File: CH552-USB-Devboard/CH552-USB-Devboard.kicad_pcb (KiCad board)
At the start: 2 copper layers, 22 x 40.5 mm, 28 parts, among them J1 Conn_01x11_Male, J2 Conn_01x11_Male, J3 USB_C_Receptacle, Q1 CPH6337, SW1 SW_Push, SW2 SW_Push, U1 CH552T, U2 CH552G, U3 MIC5504-3.3YM5, Y1 Crystal

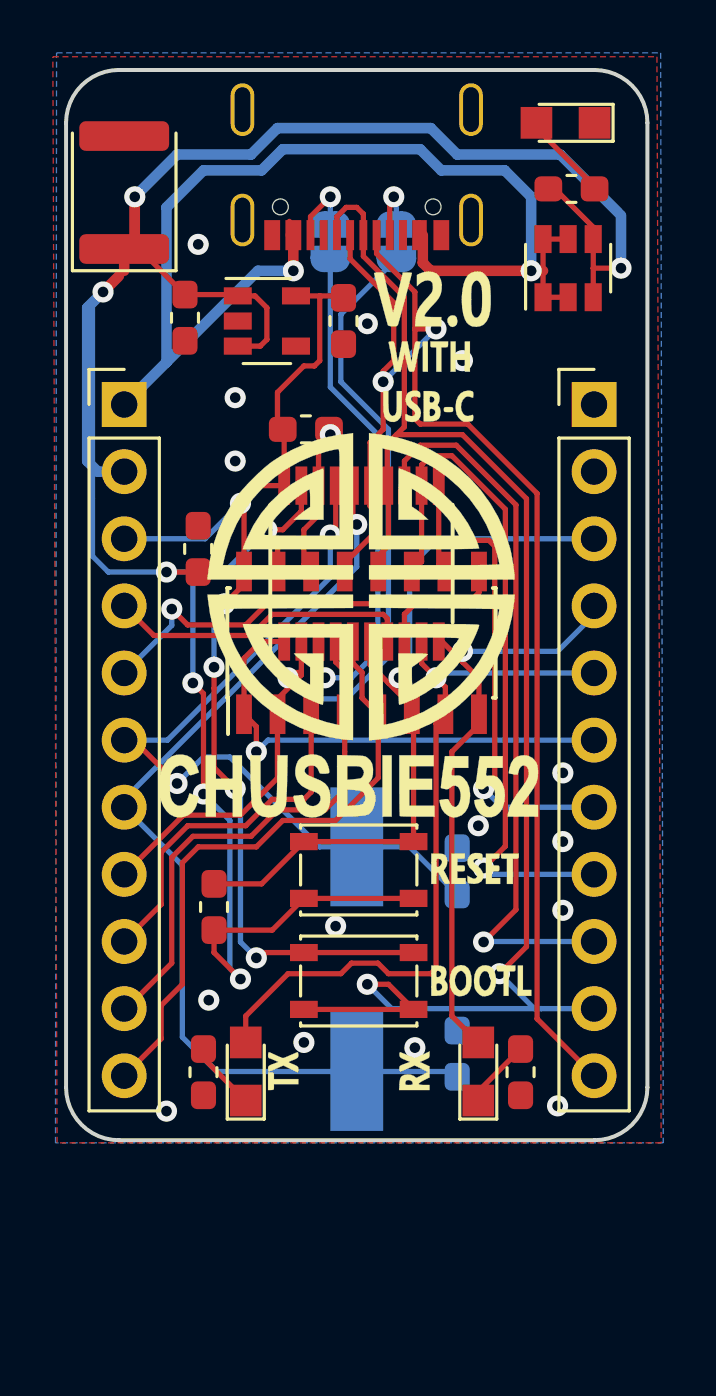
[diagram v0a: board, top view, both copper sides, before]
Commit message: add resistors for BOOTL and CC lines, remove LDO
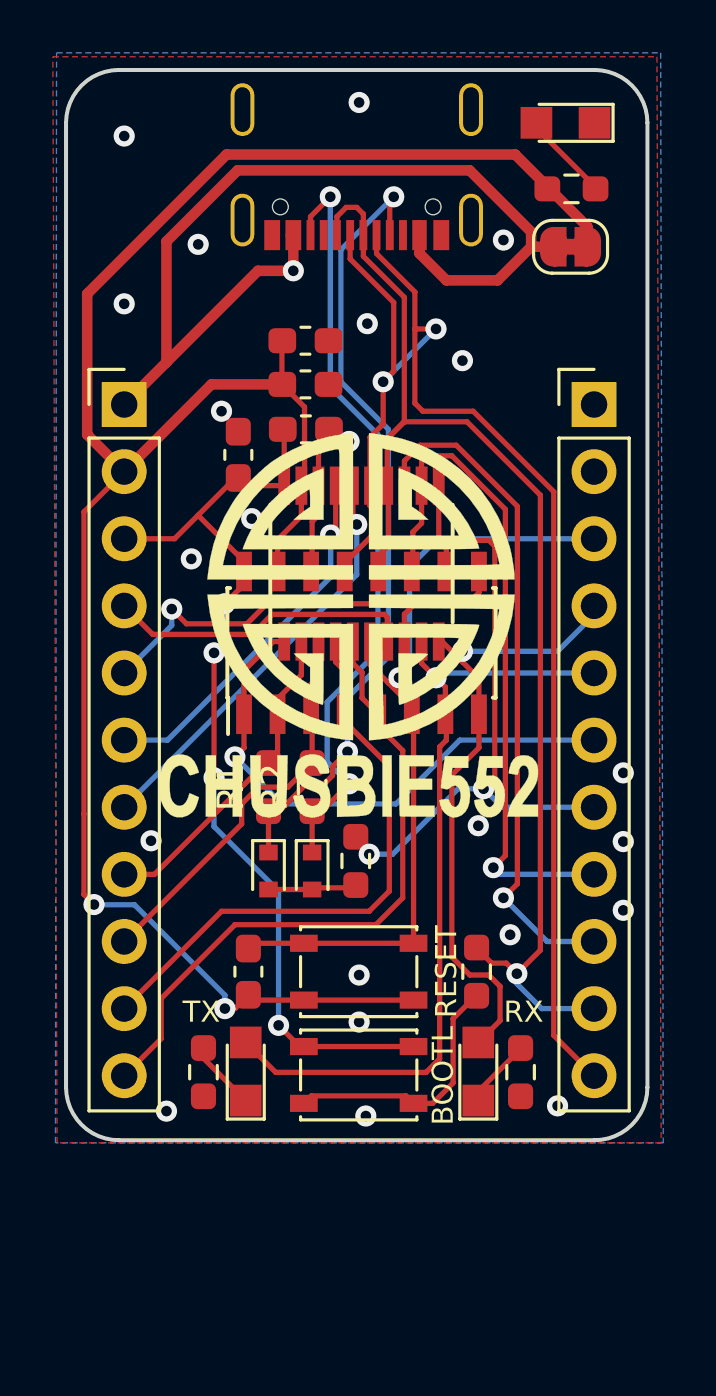
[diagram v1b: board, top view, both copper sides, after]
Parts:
- removed C5, C6: 100uF, Capacitor_SMD:C_0603_1608Metric_Pad1.05x0.95mm_HandSolder
- removed JP2: Jumper, Jumper:SolderJumper-2_P1.3mm_Bridged_RoundedPad1.0x1.5mm
- removed Q1: CPH6337, TO_SOT_Packages_SMD:SOT-23-6
- removed U3: MIC5504-3.3YM5, Package_TO_SOT_SMD:SOT-23-5
- removed Y1: Crystal, Crystal:Crystal_SMD_HC49-SD
- added D5: e.g. 1N4148, C917006, C708767, Diode_SMD:D_SOD-523, F.Cu at (83.3, 91.3)
- added R1: 68, Resistor_SMD:R_0603_1608Metric_Pad0.98x0.95mm_HandSolder, F.Cu at (81.7, 88.1)
- added R2: 68, Resistor_SMD:R_0603_1608Metric_Pad0.98x0.95mm_HandSolder, F.Cu at (83.3, 88.1)
- added R6: 22k, Resistor_SMD:R_0603_1608Metric_Pad0.98x0.95mm_HandSolder, F.Cu at (89.5, 95.1)
- added R7: 220, Resistor_SMD:R_0603_1608Metric_Pad0.98x0.95mm_HandSolder, F.Cu at (85.0, 90.9)
- C3: value 100uF -> 100nF
- C4, C7: value 1uF -> DNP/1uF
- D4: value D_ALT -> e.g. 1N4148, C917006, C708767; footprint Diode_SMD:D_1812_4532Metric -> Diode_SMD:D_SOD-523
- JP1: moved to F.Cu
- R3, R4: value 330r -> 1k; footprint Resistor_SMD:R_0603_1608Metric_Pad1.05x0.95mm_HandSolder -> Resistor_SMD:R_0603_1608Metric_Pad0.98x0.95mm_HandSolder
- R5: value 300r -> 1k; footprint Resistor_SMD:R_0603_1608Metric_Pad1.05x0.95mm_HandSolder -> Resistor_SMD:R_0603_1608Metric_Pad0.98x0.95mm_HandSolder
- moved D4 26.2 mm to (81.7, 91.3), turned to 270 degrees
- moved C1 7.43 mm to (83.1, 72.9), turned to 0 degrees
- moved JP1 6.59 mm to (93.1, 67.7), turned to 0 degrees
- moved C7 6.44 mm to (80.5, 75.6), turned to 90 degrees
- moved C4 4.64 mm to (83.1, 71.2), turned to 0 degrees
- moved SW2 3.85 mm to (85.1, 95.1)
- moved SW1 3.56 mm to (85.1, 99.0)
- moved C3 2.77 mm to (80.9, 95.1)
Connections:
- D4 pad 1: VCC -> /CC1
- D4 pad 2: GND -> Net-(D4-Pad2)
- J3 pad 1: GND -> (no net)
- JP1 pad 1: /CC1 -> VBUS
- JP1 pad 2: /P1.4 -> VCC
- SW1 pad 2: /P3.6 -> Net-(R6-Pad2)
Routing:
- net /CC1: track 2.75 -> 30.4 mm, vias 1 -> 2
- net /CC2: track 2.81 -> 29.3 mm, vias 1 -> 2
- net VCC: track 104.3 -> 78.9 mm, vias 8 -> 2
- net /P1.4: track 34.9 -> 12.3 mm, vias 1 -> 0
- net /P1.3: track 36.5 -> 15.9 mm
- net /P1.5: track 34.6 -> 15.1 mm, vias 1 -> 0
- net /P1.2: track 30.6 -> 13.9 mm, vias 2 -> 1
- net /P3.6: track 58.8 -> 47.9 mm, vias 2 -> 1
- net Net-(R6-Pad2): track 0.00 -> 9.89 mm
- net VBUS: track 46.0 -> 39.5 mm, vias 2 -> 1
- net /P3.3: track 19.4 -> 25.6 mm, vias 1 -> 2
- net +3V3: track 41.5 -> 36.0 mm, vias 5 -> 4
- net Net-(D4-Pad2): track 0.00 -> 3.38 mm
- net /P1.6: track 19.9 -> 22.2 mm
- net /P3.2: track 18.5 -> 20.7 mm
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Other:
- board text added: "BOOTL"
- board text added: "RESET"
- board text added: "RX"
- board text added: "TX"

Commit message: add reference voltage for ACMP, replace symbol for USB connector
That symbol was causing warnings because some of the pins are not
available on the footprint. Kicad has the appropriate symbol so
let's use that.
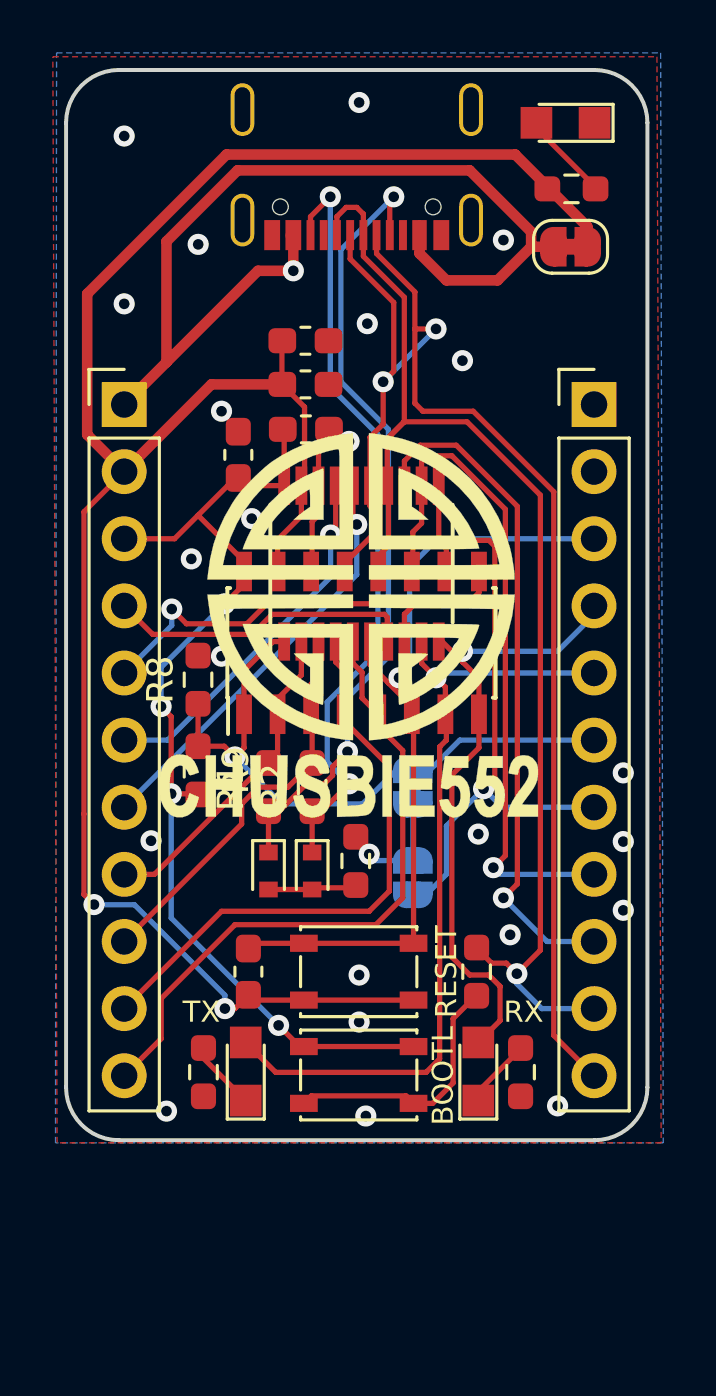
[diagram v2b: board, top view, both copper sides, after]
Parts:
- added JP2: Jumper, Jumper:SolderJumper-2_P1.3mm_Bridged_RoundedPad1.0x1.5mm, B.Cu at (87.1, 88.1)
- added JP3: Jumper, Jumper:SolderJumper-2_P1.3mm_Open_RoundedPad1.0x1.5mm, B.Cu at (87.1, 91.6)
- added R8: 1k, Resistor_SMD:R_0603_1608Metric_Pad0.98x0.95mm_HandSolder, F.Cu at (79.0, 84.1)
- added R9: 10k, Resistor_SMD:R_0603_1608Metric_Pad0.98x0.95mm_HandSolder, F.Cu at (79.0, 87.5)
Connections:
- R7 pad 1: /P3.3 -> Net-(JP2-Pad1)
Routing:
- net Net-(JP2-Pad1): track 0.00 -> 4.76 mm, vias 0 -> 1
- net /P3.2: track 20.7 -> 23.9 mm
- net +3V3: track 36.0 -> 38.7 mm
- net /P3.3: track 25.6 -> 24.8 mm, vias 2 -> 1
- net GND: vias 22 -> 23

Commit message: add voltage divider for VBUS, optimize GND plane
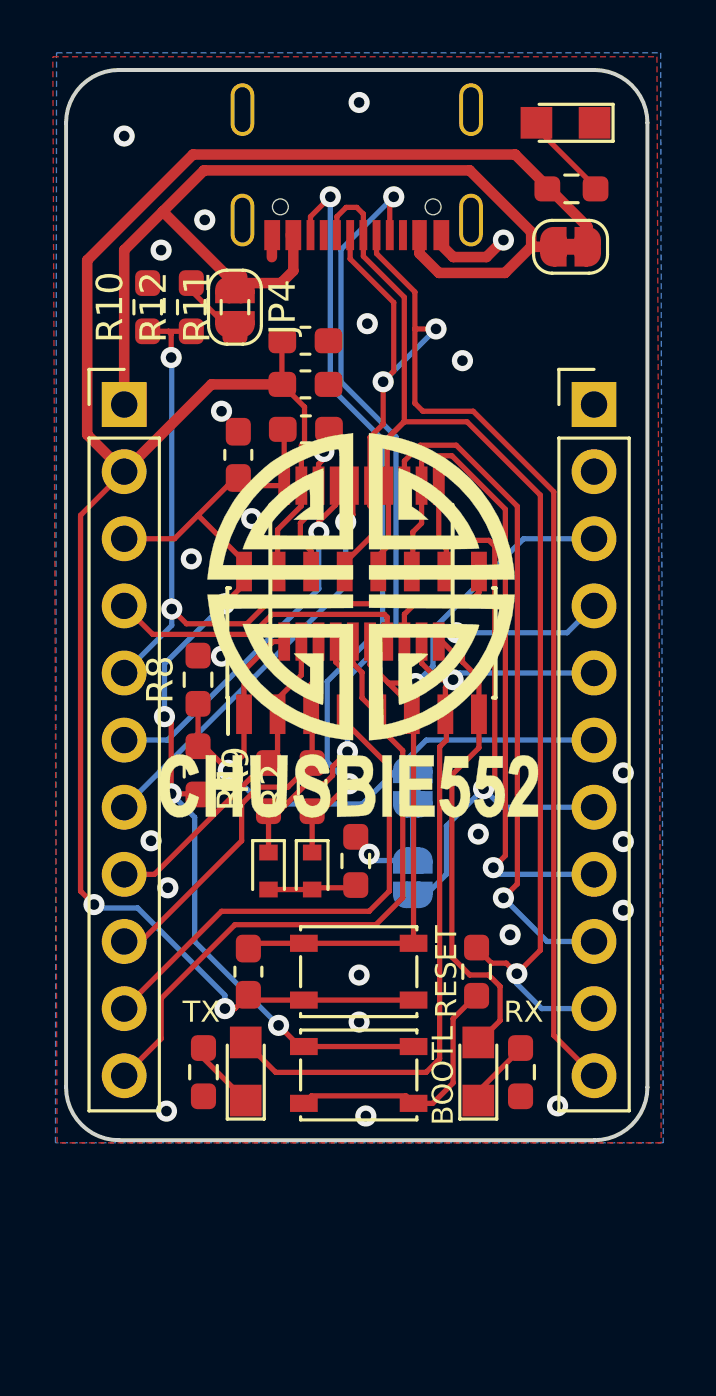
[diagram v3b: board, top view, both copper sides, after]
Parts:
- added JP4: Jumper, Jumper:SolderJumper-2_P1.3mm_Open_RoundedPad1.0x1.5mm, F.Cu at (80.4, 70.0)
- added R10: 1k, Resistor_SMD:R_0603_1608Metric_Pad0.98x0.95mm_HandSolder, F.Cu at (77.1, 70.0)
- added R11: 22k, Resistor_SMD:R_0603_1608Metric_Pad0.98x0.95mm_HandSolder, F.Cu at (80.4, 70.0)
- added R12: 22k, Resistor_SMD:R_0603_1608Metric_Pad0.98x0.95mm_HandSolder, F.Cu at (78.7, 70.0)
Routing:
- net /P1.1: track 17.9 -> 30.1 mm, vias 1 -> 2
- net GND: track 5.48 -> 9.82 mm, vias 23 -> 24
- net Net-(JP4-Pad2): track 0.00 -> 2.55 mm
- net /RESET: track 30.6 -> 29.2 mm
- net /P3.2: track 23.9 -> 25.0 mm
- net VCC: track 78.9 -> 79.7 mm
- net /P3.0: track 24.1 -> 24.6 mm
- net VBUS: track 39.5 -> 40.0 mm, vias 1 -> 0

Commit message: add 2nd USB connector, dedicated to PD monitoring
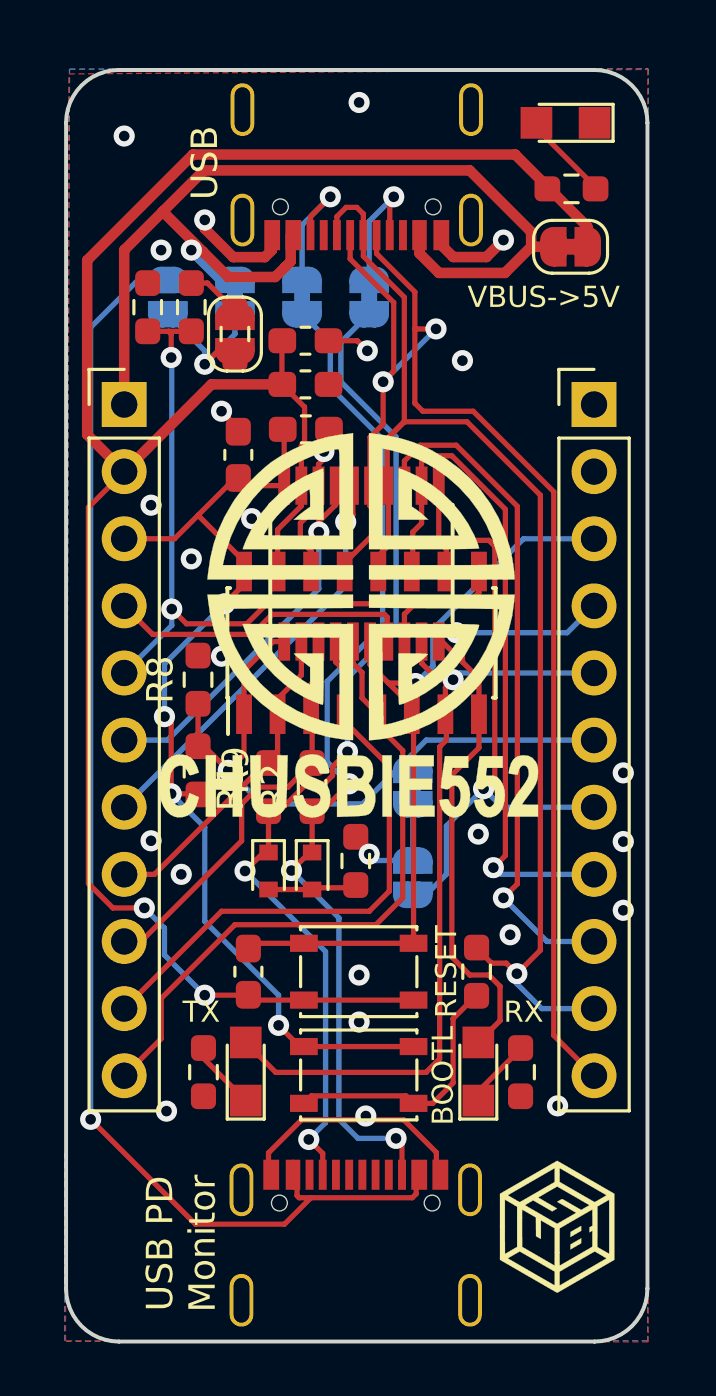
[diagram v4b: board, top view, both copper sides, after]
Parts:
- added G***: LOGO, Glowstone:subraum_8mm, B.Cu at (85.0, 105.0)
- added G***: LOGO, Glowstone:subraum_5mm, F.Cu at (92.6, 104.8)
- added J4: USB_C_Receptacle, footprint:VACON_CSP_USC16_TR, F.Cu at (85.0, 103.4)
- added JP5: Jumper, Jumper:SolderJumper-2_P1.3mm_Bridged_RoundedPad1.0x1.5mm, B.Cu at (85.5, 69.6)
- added JP6: Jumper, Jumper:SolderJumper-2_P1.3mm_Bridged_RoundedPad1.0x1.5mm, B.Cu at (82.9, 69.6)
- added JP7: Jumper, Jumper:SolderJumper-2_P1.3mm_Bridged_RoundedPad1.0x1.5mm, B.Cu at (80.4, 69.6)
- added JP8: Jumper, Jumper:SolderJumper-2_P1.3mm_Open_RoundedPad1.0x1.5mm, B.Cu at (77.9, 69.6)
- moved JP4 1.02 mm to (80.4, 71.0), turned to 90 degrees
- moved R11 1.02 mm to (80.4, 71.0), turned to 270 degrees
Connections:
- J3 pad A5: /CC1 -> Net-(J3-PadA5)
- J3 pad B5: /CC2 -> Net-(J3-PadB5)
- JP4 pad 1: VBUS -> Net-(JP4-Pad1)
- R11 pad 2: VBUS -> Net-(JP4-Pad1)
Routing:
- net /VBUS2: track 0.00 -> 50.8 mm, vias 0 -> 1
- net GND: track 9.82 -> 25.4 mm
- net /CC2: track 29.5 -> 38.9 mm, vias 2 -> 3
- net /CC1: track 30.7 -> 38.8 mm, vias 2 -> 3
- net Net-(JP4-Pad1): track 0.00 -> 6.20 mm, vias 0 -> 1
- net Net-(J3-PadB5): track 0.00 -> 5.36 mm, vias 0 -> 1
- net Net-(J3-PadA5): track 0.00 -> 4.93 mm, vias 0 -> 1
- net VBUS: track 40.0 -> 40.9 mm, vias 0 -> 1
- net (no net): vias 0 -> 1
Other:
- board size 22 x 40.5 mm -> 22 x 48.1 mm
- board text added: "CC lines"
- board text added: "CC-OUT= P3.2 P3.3"
- board text added: "USB"
- board text added: "USB PD Monitor"
- board text added: "VBUS->5V"
- board text added: "VBUS1"
- board text added: "VBUS2"

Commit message: update PCB
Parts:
- removed the G*** at (84.7, 84.1)
- removed JP4: Jumper, Jumper:SolderJumper-2_P1.3mm_Open_RoundedPad1.0x1.5mm
- added C10: 10uF, Capacitor_SMD:C_0603_1608Metric_Pad1.05x0.95mm_HandSolder, F.Cu at (83.2, 73.3)
- added C5: 4u7, 50V, Capacitor_SMD:C_1206_3216Metric_Pad1.42x1.75mm_HandSolder, F.Cu at (93.0, 69.5)
- added C6: 4u7, 50V, Capacitor_SMD:C_1206_3216Metric_Pad1.42x1.75mm_HandSolder, F.Cu at (87.9, 69.5)
- added C8: 10nF, Capacitor_SMD:C_0603_1608Metric_Pad1.05x0.95mm_HandSolder, F.Cu at (90.4, 78.0)
- added C9: 100nF, Capacitor_SMD:C_0603_1608Metric_Pad1.05x0.95mm_HandSolder, F.Cu at (84.3, 70.7)
- added R13: 22k, Resistor_SMD:R_0603_1608Metric_Pad1.05x0.95mm_HandSolder, F.Cu at (90.4, 74.9)
- added R14: DNP / 68k, Resistor_SMD:R_0603_1608Metric_Pad1.05x0.95mm_HandSolder, F.Cu at (90.4, 76.5)
- added U3: TPS7A4101DGNT, CH552-USB-Devboard:HVSSOP-8_3.0x3.0mm_P0.65mm, F.Cu at (88.6, 72.4)
- D1, D2: value LED -> LED, yellow
- D3: value LED -> LED, green?
- D4, D5: footprint Diode_SMD:D_SOD-523 -> Diode_SMD:D_SOD-323F
- JP1: footprint Jumper:SolderJumper-2_P1.3mm_Bridged_RoundedPad1.0x1.5mm -> Jumper:SolderJumper-2_P1.3mm_Open_RoundedPad1.0x1.5mm
- R11: value 22k -> 62k; footprint Resistor_SMD:R_0603_1608Metric_Pad0.98x0.95mm_HandSolder -> Resistor_SMD:R_0603_1608Metric_Pad1.05x0.95mm_HandSolder
- R12: value 22k -> 10k
- R3, R4, R5: value 1k -> 10k
- moved R11 11.4 mm to (90.4, 76.5), turned to 180 degrees
- moved C1 3.32 mm to (79.8, 73.3), turned to 180 degrees
- moved C4 2.09 mm to (81.0, 71.8), turned to 180 degrees
- moved JP5 1.78 mm to (85.6, 67.8)
- moved C7 1.67 mm to (80.8, 77.2)
- moved R6 1.02 mm to (90.4, 95.6), turned to 180 degrees
- moved C2 0.81 mm to (82.3, 74.8)
- moved JP1 0.76 mm to (93.1, 66.9)
- moved R5 0.76 mm to (93.1, 64.7)
- moved R7 0.52 mm to (85.1, 91.4)
- moved JP6 0.51 mm to (82.9, 69.1)
- moved JP8 0.38 mm to (77.5, 69.6), turned to 90 degrees
- moved D4 0.28 mm to (81.4, 91.4)
- moved D5 0.13 mm to (83.3, 91.4)
- moved R10 0.13 mm to (77.0, 70.0)
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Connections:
- JP7 pad 2: Net-(JP4-Pad1) -> Net-(JP7-Pad2)
- JP8 pad 2: Net-(JP4-Pad1) -> Net-(JP7-Pad2)
- R11 pad 1: Net-(JP4-Pad2) -> Net-(C8-Pad2)
- R11 pad 2: Net-(JP4-Pad1) -> VCC
- R12 pad 2: Net-(JP4-Pad2) -> Net-(JP7-Pad2)
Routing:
- net GND: track 25.4 -> 96.5 mm, vias 24 -> 41
- net VCC: track 79.3 -> 93.7 mm, vias 2 -> 4
- net Net-(C8-Pad2): track 0.00 -> 13.6 mm, vias 0 -> 2
- net VBUS: track 40.9 -> 50.1 mm
- net /CC1: track 38.8 -> 45.8 mm, vias 3 -> 5
- net Net-(JP4-Pad1): track 6.20 -> 0.00 mm, vias 1 -> 0
- net /P3.6: track 47.9 -> 53.8 mm, vias 1 -> 3
- net /P3.3: track 24.8 -> 29.6 mm
- net Net-(JP7-Pad2): track 0.00 -> 4.17 mm, vias 0 -> 1
- net /P3.7: track 54.4 -> 50.7 mm, vias 2 -> 4
- net Net-(J3-PadB5): track 5.36 -> 1.79 mm
- net /RESET: track 29.2 -> 32.3 mm
- net Net-(JP4-Pad2): track 2.34 -> 0.00 mm
- net /P3.4: track 26.1 -> 23.9 mm, vias 1 -> 3
- net Net-(C5-Pad2): track 0.00 -> 2.11 mm
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
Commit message: some small changes for the PCB
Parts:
- moved D3 0.38 mm to (92.5, 63.0)
- moved JP1 0.38 mm to (92.7, 66.9)
- moved R5 0.38 mm to (92.7, 64.7)
- moved G*** 0.25 mm to (85.0, 104.8)
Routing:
- net GND: vias 41 -> 45
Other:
- board text added: "CC-OUT="
- board text added: "P3.2 P3.3"
- board text added: "VBUS=5V"
- board text removed: "CC-OUT= P3.2 P3.3"
- board text removed: "VBUS->5V"
